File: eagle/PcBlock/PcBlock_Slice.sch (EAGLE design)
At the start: 10 parts

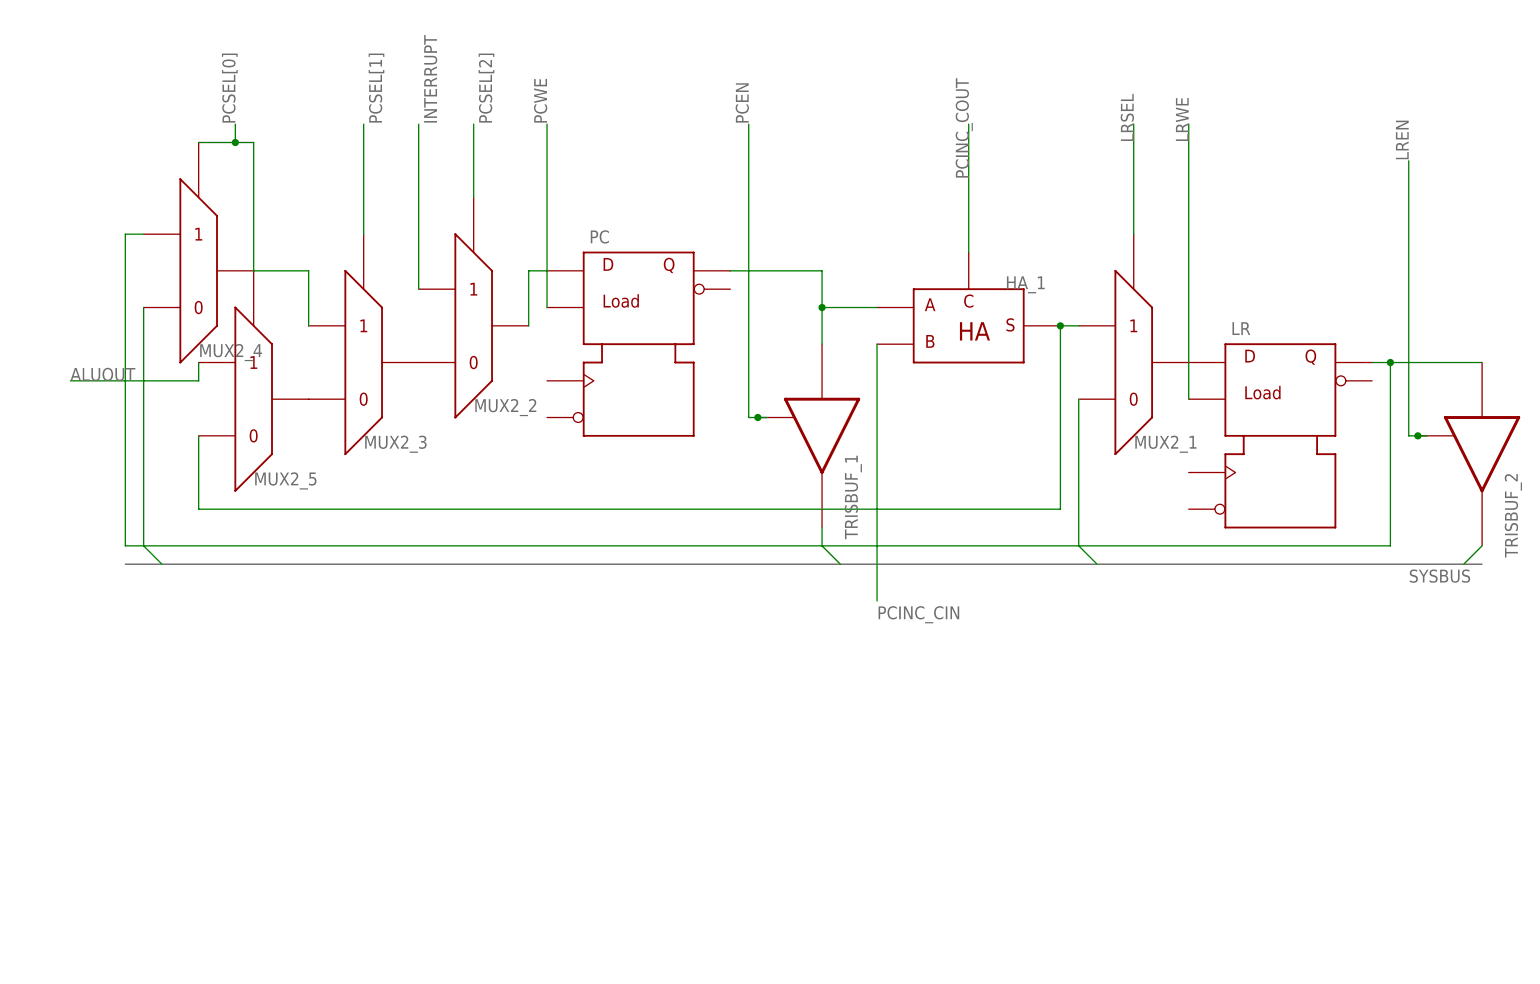
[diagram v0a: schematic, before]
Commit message: Added figure and a little more text to Pc section #96
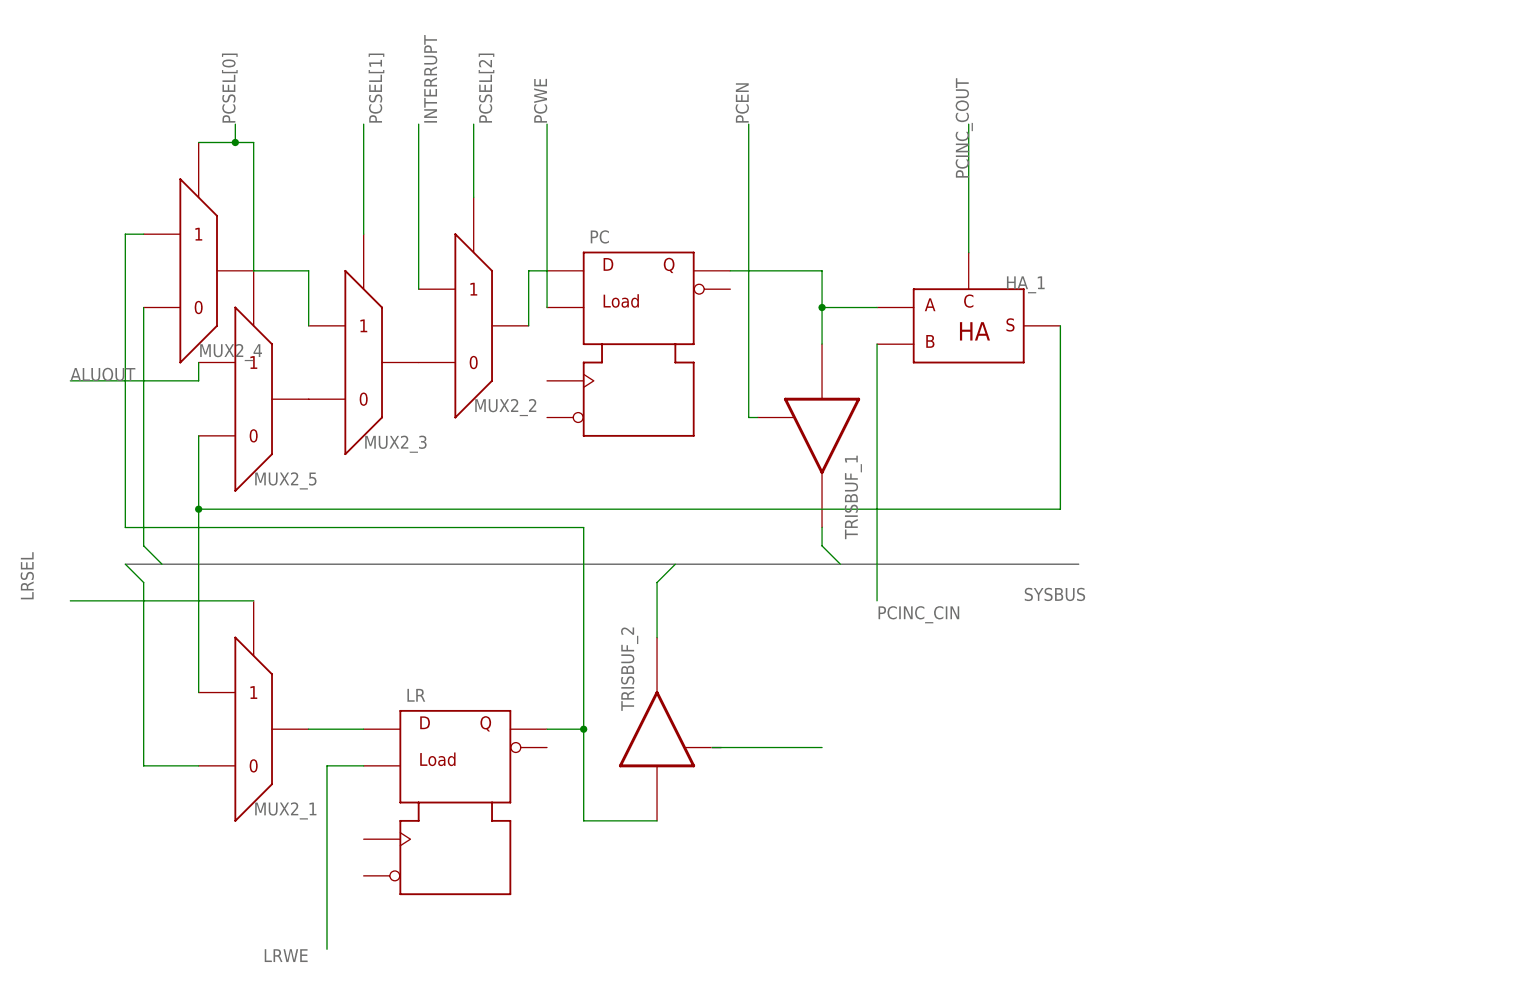
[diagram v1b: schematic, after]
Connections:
- removed net LREN: TRISBUF_2.P$1
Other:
- moved on the sheet: LR, MUX2_1, TRISBUF_2
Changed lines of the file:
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@@
 <instances>
 <instance part="PC" gate="G$1" x="71.12" y="40.64"/>
-<instance part="LR" gate="G$1" x="160.02" y="27.94"/>
+<instance part="LR" gate="G$1" x="45.72" y="-22.86"/>
 <instance part="TRISBUF_1" gate="G$1" x="96.52" y="22.86" rot="R270"/>
-<instance part="TRISBUF_2" gate="G$1" x="187.96" y="20.32" rot="R270"/>
-<instance part="MUX2_1" gate="G$1" x="142.24" y="33.02" rot="MR180"/>
+<instance part="TRISBUF_2" gate="G$1" x="73.66" y="-17.78" rot="R90"/>
+<instance part="MUX2_1" gate="G$1" x="20.32" y="-17.78" rot="MR180"/>
 <instance part="MUX2_2" gate="G$1" x="50.8" y="38.1" rot="MR180"/>
 <instance part="MUX2_3" gate="G$1" x="35.56" y="33.02" rot="MR180"/>
@@
 <bus name="SYSBUS">
 <segment>
-<wire x1="0" y1="5.08" x2="187.96" y2="5.08" width="0.762" layer="92"/>
-<label x="177.8" y="2.54" size="1.778" layer="95"/>
+<wire x1="0" y1="5.08" x2="132.08" y2="5.08" width="0.762" layer="92"/>
+<label x="124.46" y="0" size="1.778" layer="95"/>
 </segment>
 </bus>
 </busses>
 <nets>
-<net name="N$1" class="0">
-<segment>
-<pinref part="LR" gate="G$1" pin="Q"/>
-<pinref part="TRISBUF_2" gate="G$1" pin="I"/>
-<wire x1="172.72" y1="33.02" x2="175.26" y2="33.02" width="0.1524" layer="91"/>
-<wire x1="175.26" y1="33.02" x2="187.96" y2="33.02" width="0.1524" layer="91"/>
-<wire x1="0" y1="7.62" x2="175.26" y2="7.62" width="0.1524" layer="91"/>
-<wire x1="175.26" y1="7.62" x2="175.26" y2="33.02" width="0.1524" layer="91"/>
-<junction x="175.26" y="33.02"/>
-<pinref part="MUX2_4" gate="G$1" pin="P$2"/>
-<wire x1="2.54" y1="50.8" x2="0" y2="50.8" width="0.1524" layer="91"/>
-<wire x1="0" y1="50.8" x2="0" y2="7.62" width="0.1524" layer="91"/>
-</segment>
-</net>
 <net name="SYSBUS" class="0">
 <segment>
@@
 </segment>
 <segment>
-<pinref part="TRISBUF_2" gate="G$1" pin="O"/>
-<wire x1="187.96" y1="7.62" x2="185.42" y2="5.08" width="0.1524" layer="91"/>
-</segment>
-<segment>
 <pinref part="MUX2_1" gate="G$1" pin="P$1"/>
-<wire x1="132.08" y1="27.94" x2="132.08" y2="7.62" width="0.1524" layer="91"/>
-<wire x1="132.08" y1="7.62" x2="134.62" y2="5.08" width="0.1524" layer="91"/>
+<wire x1="10.16" y1="-22.86" x2="2.54" y2="-22.86" width="0.1524" layer="91"/>
+<wire x1="2.54" y1="-22.86" x2="2.54" y2="2.54" width="0.1524" layer="91"/>
+<wire x1="2.54" y1="2.54" x2="0" y2="5.08" width="0.1524" layer="91"/>
 </segment>
 <segment>
@@
 <wire x1="2.54" y1="7.62" x2="5.08" y2="5.08" width="0.1524" layer="91"/>
 </segment>
+<segment>
+<pinref part="TRISBUF_2" gate="G$1" pin="O"/>
+<wire x1="73.66" y1="-5.08" x2="73.66" y2="2.54" width="0.1524" layer="91"/>
+<wire x1="73.66" y1="2.54" x2="76.2" y2="5.08" width="0.1524" layer="91"/>
+</segment>
 </net>
 <net name="N$3" class="0">
@@
 <pinref part="LR" gate="G$1" pin="D"/>
 <pinref part="MUX2_1" gate="G$1" pin="P$3"/>
+<wire x1="25.4" y1="-17.78" x2="33.02" y2="-17.78" width="0.1524" layer="91"/>
 </segment>
 </net>
@@
 <net name="N$7" class="0">
 <segment>
-<pinref part="MUX2_1" gate="G$1" pin="P$2"/>
 <pinref part="HA_1" gate="G$1" pin="S"/>
 <pinref part="MUX2_5" gate="G$1" pin="P$1"/>
@@
 <wire x1="10.16" y1="12.7" x2="129.54" y2="12.7" width="0.1524" layer="91"/>
 <wire x1="129.54" y1="12.7" x2="129.54" y2="38.1" width="0.1524" layer="91"/>
-<junction x="129.54" y="38.1"/>
-<wire x1="129.54" y1="38.1" x2="132.08" y2="38.1" width="0.1524" layer="91"/>
+<pinref part="MUX2_1" gate="G$1" pin="P$2"/>
+<wire x1="10.16" y1="-12.7" x2="10.16" y2="12.7" width="0.1524" layer="91"/>
+<junction x="10.16" y="12.7"/>
 </segment>
 </net>
@@
 <net name="PCEN" class="0">
 <segment>
-<wire x1="88.9" y1="25.4" x2="87.63" y2="25.4" width="0.1524" layer="91"/>
 <wire x1="87.63" y1="25.4" x2="86.36" y2="25.4" width="0.1524" layer="91"/>
 <wire x1="86.36" y1="25.4" x2="86.36" y2="66.04" width="0.1524" layer="91"/>
 <label x="86.36" y="66.04" size="1.778" layer="95" rot="R90"/>
 <pinref part="TRISBUF_1" gate="G$1" pin="P$1"/>
-<junction x="87.63" y="25.4"/>
 </segment>
 </net>
@@
 <segment>
 <pinref part="MUX2_1" gate="G$1" pin="P$4"/>
-<wire x1="139.7" y1="50.8" x2="139.7" y2="66.04" width="0.1524" layer="91"/>
-<label x="139.7" y="63.5" size="1.778" layer="95" rot="R90"/>
+<wire x1="17.78" y1="0" x2="-7.62" y2="0" width="0.1524" layer="91"/>
+<label x="-12.7" y="0" size="1.778" layer="95" rot="R90"/>
 </segment>
 </net>
@@
 </segment>
 </net>
-<net name="LREN" class="0">
-<segment>
-<wire x1="180.34" y1="22.86" x2="179.07" y2="22.86" width="0.1524" layer="91"/>
-<wire x1="179.07" y1="22.86" x2="177.8" y2="22.86" width="0.1524" layer="91"/>
-<wire x1="177.8" y1="22.86" x2="177.8" y2="60.96" width="0.1524" layer="91"/>
-<label x="177.8" y="60.96" size="1.778" layer="95" rot="R90"/>
-<pinref part="TRISBUF_2" gate="G$1" pin="P$1"/>
-<junction x="179.07" y="22.86"/>
-</segment>
-</net>
 <net name="PCWE" class="0">
 <segment>
@@
 <segment>
 <pinref part="LR" gate="G$1" pin="LOAD"/>
-<wire x1="147.32" y1="27.94" x2="147.32" y2="66.04" width="0.1524" layer="91"/>
-<label x="147.32" y="63.5" size="1.778" layer="95" rot="R90"/>
-</segment>
-</net>
+<wire x1="33.02" y1="-22.86" x2="27.94" y2="-22.86" width="0.1524" layer="91"/>
+<wire x1="27.94" y1="-22.86" x2="27.94" y2="-48.26" width="0.1524" layer="91"/>
+<label x="25.4" y="-48.26" size="1.778" layer="95" rot="R180"/>
+</segment>
+</net>
+<net name="N$9" class="0">
+<segment>
+<wire x1="81.28" y1="-20.32" x2="96.52" y2="-20.32" width="0.1524" layer="91"/>
+</segment>
+</net>
+<net name="N$10" class="0">
+<segment>
+<pinref part="TRISBUF_2" gate="G$1" pin="I"/>
+<wire x1="73.66" y1="-30.48" x2="63.5" y2="-30.48" width="0.1524" layer="91"/>
+<wire x1="63.5" y1="-30.48" x2="63.5" y2="-17.78" width="0.1524" layer="91"/>
+<pinref part="LR" gate="G$1" pin="Q"/>
+<wire x1="63.5" y1="-17.78" x2="58.42" y2="-17.78" width="0.1524" layer="91"/>
+<wire x1="0" y1="10.16" x2="63.5" y2="10.16" width="0.1524" layer="91"/>
+<pinref part="MUX2_4" gate="G$1" pin="P$2"/>
+<wire x1="2.54" y1="50.8" x2="0" y2="50.8" width="0.1524" layer="91"/>
+<wire x1="0" y1="50.8" x2="0" y2="10.16" width="0.1524" layer="91"/>
+<wire x1="63.5" y1="-17.78" x2="63.5" y2="10.16" width="0.1524" layer="91"/>
+<junction x="63.5" y="-17.78"/>
+</segment>
+</net>
